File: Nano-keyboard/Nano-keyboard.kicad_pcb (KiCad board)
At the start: 2 copper layers, 130 x 77 mm, 45 parts, among them J1 125SH-B-04-TS, J2 125SH-B-02-TS, U1 AMS1117, U2 ESP32-WROOM-32, U3 J5019, U4 QBC847BL, U5 EN12-HN22AF25, U6 EN12-HN22AF25, U7 QBC847BL, U8 QBC847BL

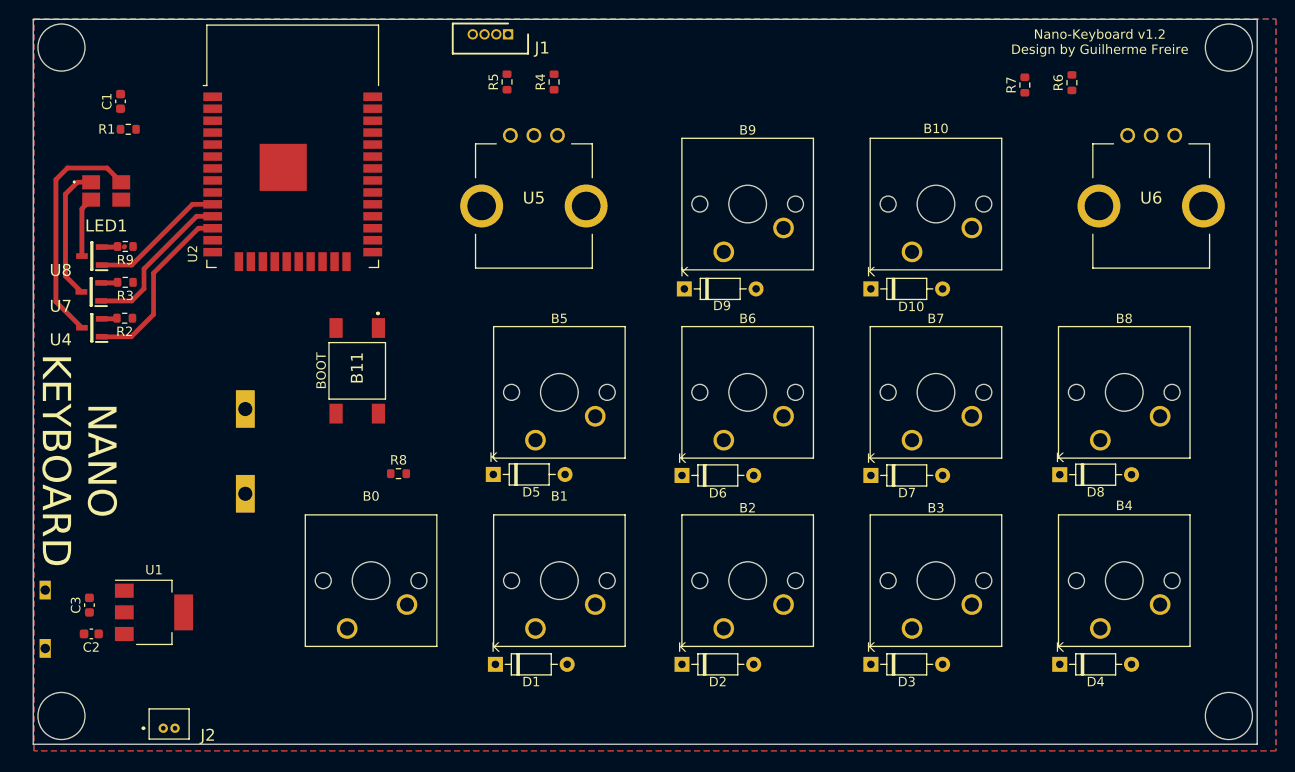
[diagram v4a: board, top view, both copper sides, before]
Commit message: Routing of version 1.2 almest finished
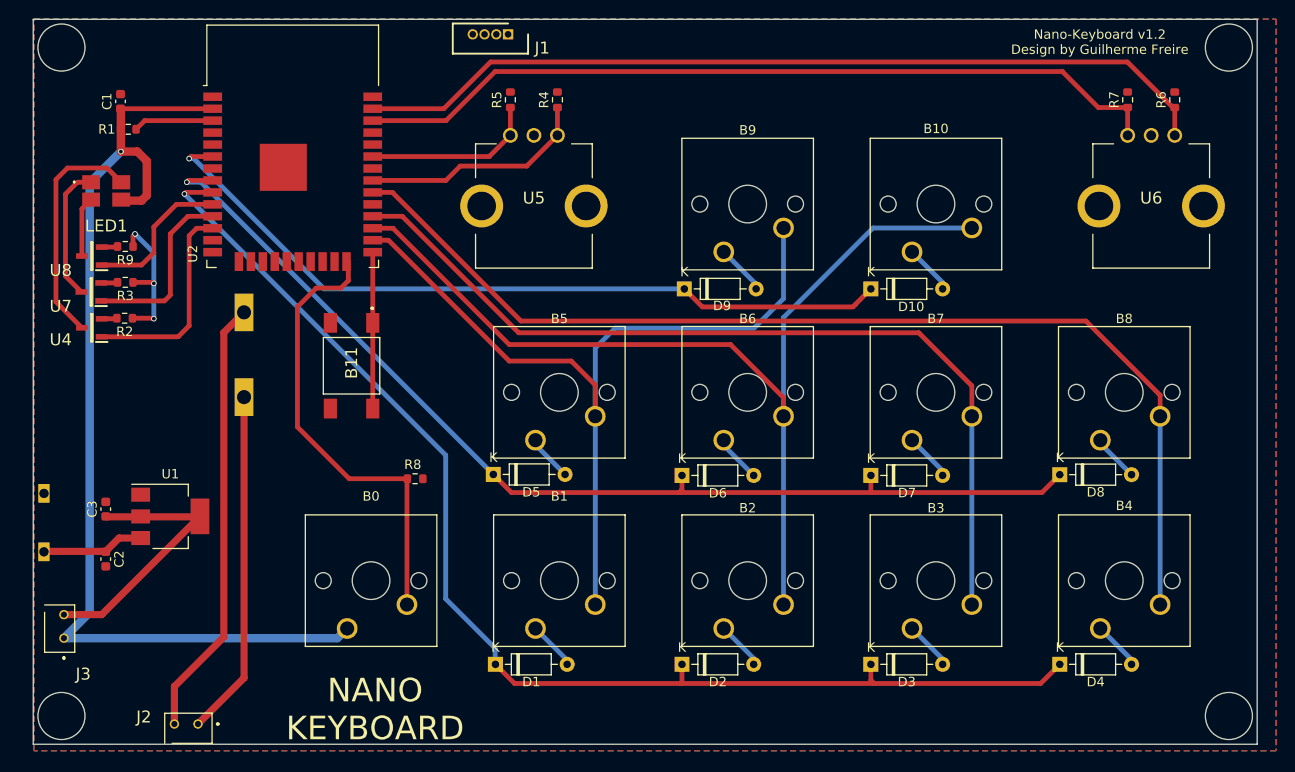
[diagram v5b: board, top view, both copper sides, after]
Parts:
- added J3: 25SH-B-02-TS, lib:25SHB02TS, F.Cu at (69.9, 130.5)
- J2: value 125SH-B-02-TS -> 25SH-B-02-TS; footprint lib:125SHB02TS -> lib:25SHB02TS
- moved R6 11.1 mm to (187.9, 73.3)
- moved R7 11.0 mm to (182.9, 73.3)
- moved U1 10.3 mm to (81.2, 117.6)
- moved C3 10.3 mm to (74.4, 116.8)
- moved U3 10.3 mm to (90.8, 122.8)
- moved C2 8.09 mm to (74.4, 122.1), turned to -90 degrees
- moved J2 3.71 mm to (84.2, 139.6), turned to 0 degrees
- moved R4 1.93 mm to (122.4, 73.3)
- moved R5 1.93 mm to (117.4, 73.3)
- moved R8 1.84 mm to (107.2, 113.6), turned to 180 degrees
- moved B11 0.81 mm to (100.5, 101.6)
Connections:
- C3 pad 1: +3V3 -> /MASTER_SWITCH
- U1 pad 2: +3V3 -> /MASTER_SWITCH
- U2 pad 31: /ENCODER2_B -> /ENCODER2_A
- U2 pad 33: /ENCODER2_A -> /ENCODER2_B
- U2 pad 8: ROW1 -> ROW2
- U2 pad 9: ROW2 -> ROW1
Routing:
- net ROW1: track 0.00 -> 132.7 mm, vias 0 -> 1
- net COL4: track 0.00 -> 114.8 mm
- net ROW2: track 0.00 -> 113.8 mm, vias 0 -> 1
- net +3V3: track 0.00 -> 108.7 mm, vias 0 -> 1
- net COL2: track 0.00 -> 107.5 mm
- net COL3: track 0.00 -> 94.3 mm
- net /ENCODER1_A: track 0.00 -> 92.2 mm
- net COL1: track 0.00 -> 90.3 mm
- net /ENCODER1_B: track 0.00 -> 86.9 mm
- net ROW3: track 0.00 -> 82.3 mm, vias 0 -> 1
- net /FUNC: track 0.00 -> 48.7 mm
- net Net-(J2-Pad2): track 0.00 -> 46.8 mm
- net Net-(J2-Pad1): track 0.00 -> 36.7 mm
- net /MASTER_SWITCH: track 0.00 -> 28.8 mm
- net /ENCODER2_A: track 0.00 -> 24.6 mm
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
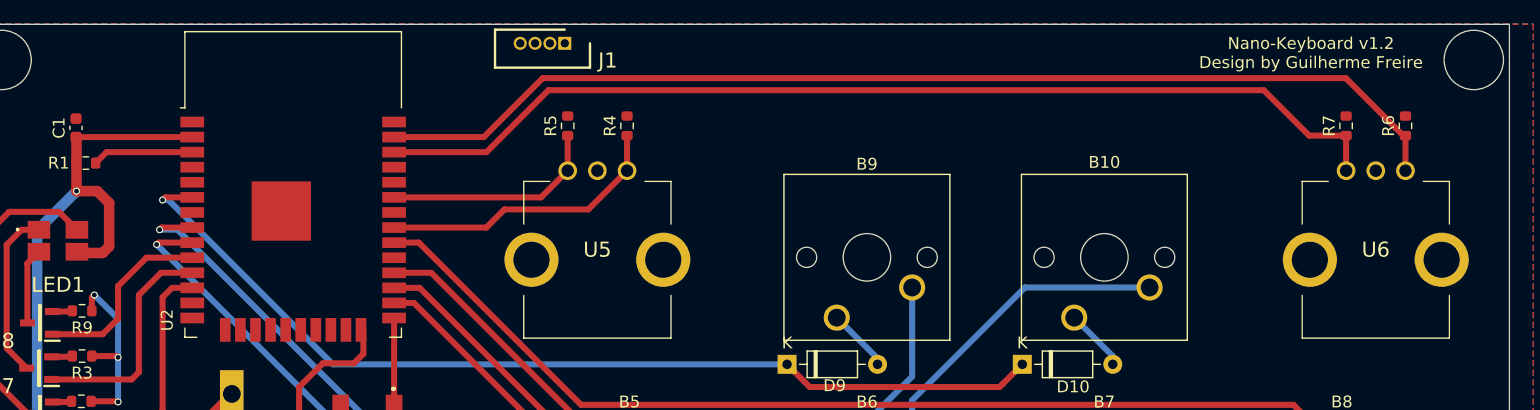
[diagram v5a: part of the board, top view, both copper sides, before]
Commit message: Finished Routing
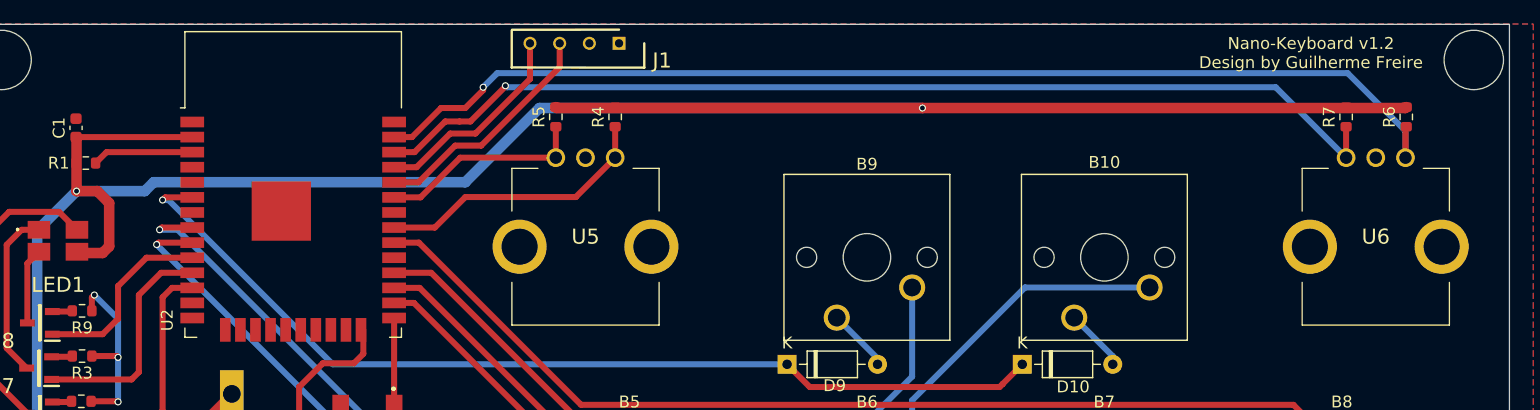
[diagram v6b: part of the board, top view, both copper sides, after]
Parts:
- moved J1 4.57 mm to (121.7, 66.4)
- moved U5 1.49 mm to (121.4, 76.0)
- moved R4 1.25 mm to (121.4, 72.6)
- moved R5 1.25 mm to (116.4, 72.6)
- moved U6 1.10 mm to (187.9, 76.0)
- moved R6 0.75 mm to (188.0, 72.6)
- moved R7 0.75 mm to (182.9, 72.6)
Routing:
- net +3V3: track 108.7 -> 254.6 mm, vias 1 -> 2
- net /RX0: track 0.00 -> 20.0 mm
- net /TX0: track 0.00 -> 17.5 mm
- net /ENCODER1_A: track 92.2 -> 94.5 mm, vias 0 -> 1
- net /ENCODER2_A: track 24.6 -> 23.7 mm
- net /ENCODER2_B: track 18.5 -> 17.6 mm
- net /ENCODER1_B: track 86.9 -> 87.7 mm, vias 0 -> 1
